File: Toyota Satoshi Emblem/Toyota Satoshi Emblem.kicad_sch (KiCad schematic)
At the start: 478 parts, among them J1 Conn_01x03_Male, J10 Ambient Harness, J11 Letter Terminal, J12 Letter Terminal, J13 Letter Terminal, J14 Letter Terminal, J15 Letter Terminal, J16 Letter Terminal, J17 Serial Terminal, J18 Power Port Terminal, J2 Conn_01x03_Male, J3 Conn_01x03_Male, J4 Conn_01x03_Male, J5 Conn_01x03_Male, J6 Conn_01x03_Male, J7 Conn_01x09_Male, J8 Conn_01x09_Female, J9 Serial Terminal, K1 FINDER-40.51, Q1 BC327, Q10 2N3904, Q11 IRLZ44N, Q12 IRLZ44N, Q13 IRLZ44N, Q14 IRLZ44N, Q15 IRLZ44N, Q16 IRLZ44N, Q17 IRLZ44N, Q18 IRLZ44N, Q19 IRLZ44N, Q2 BC337, Q20 IRLZ44N, Q21 2N3904, Q22 2N3904, Q23 2N3904, Q24 2N3904, Q25 2N3904, Q26 2N3904, Q27 IRLZ44N, Q28 IRLZ44N, Q29 IRLZ44N, Q3 IRF4905, Q30 IRLZ44N, Q31 IRLZ44N, Q32 IRLZ44N, Q33 IRLZ44N, Q34 IRLZ44N, Q35 IRLZ44N, Q36 IRLZ44N, Q37 IRLZ44N, Q38 IRLZ44N, Q4 IRLZ44N, Q5 IRLZ44N, Q6 IRLZ44N, Q7 IRLZ44N, Q8 IRLZ44N, Q9 IRLZ44N, U1 LM2596S-ADJ, U2 LM2596S-ADJ, U3 L7805, U4 LM2596S-ADJ, U5 LM2596S-ADJ

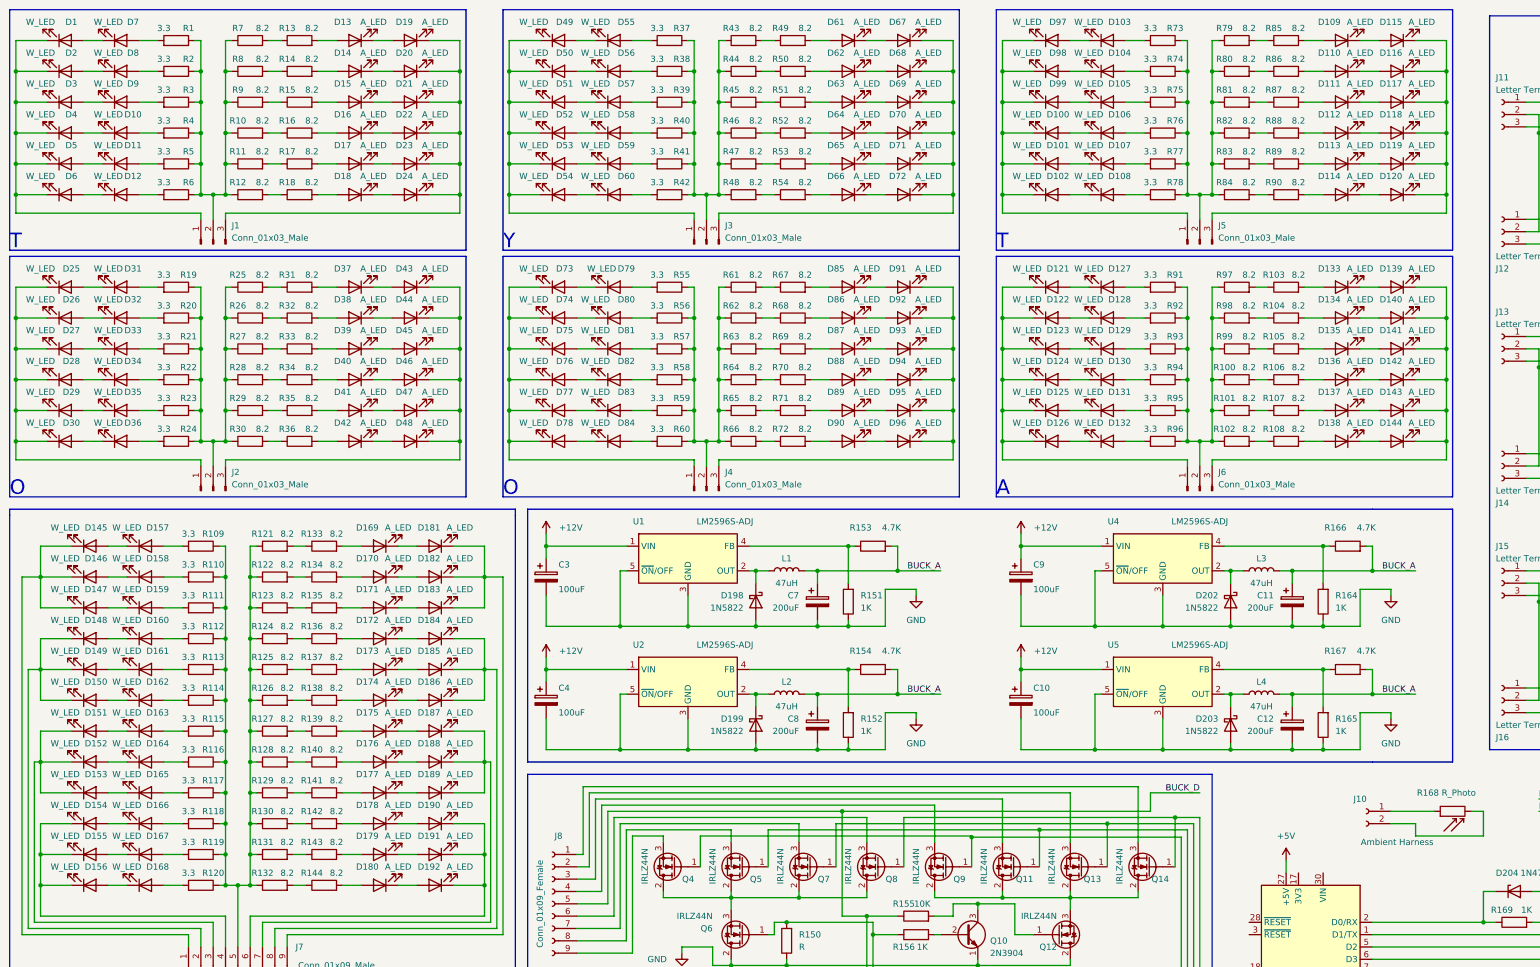
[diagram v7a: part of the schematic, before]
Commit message: v1.8
Letter T is now complete
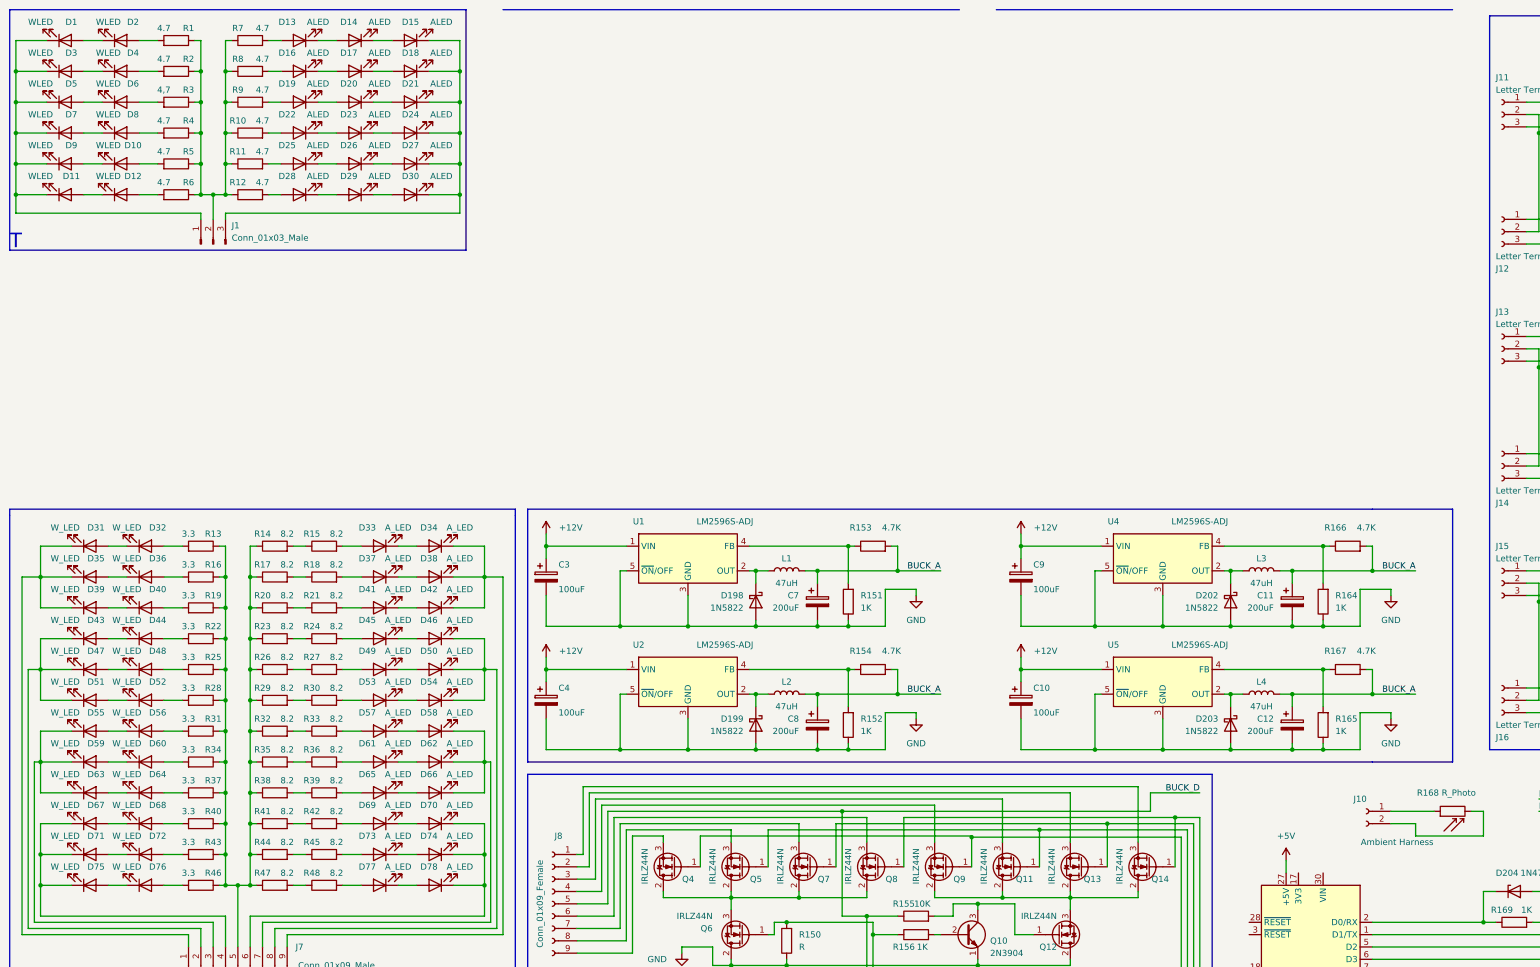
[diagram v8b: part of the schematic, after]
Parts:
- removed D100, D101, D102, D103, D104, D105, D106, D107, D108, D121, D122, D123, D124, D125, D126, D127, D128, D129, D130, D131, D132, D26, D27, D29, D30, D31, D32, D33, D34, D35, D36, D49, D50, D51, D52, D53, D54, D55, D56, D57, D58, D59, D60, D73, D74, D75, D76, D77, D78, D79, D80, D81, D82, D83, D84, D97, D98, D99: W_LED, afootprints:5730 LED W, symbol Device:LED
- removed D109, D110, D111, D112, D113, D114, D115, D116, D117, D118, D119, D120, D133, D134, D135, D136, D137, D138, D139, D140, D141, D142, D143, D144, D37, D38, D39, D40, D41, D42, D43, D44, D45, D46, D47, D48, D61, D62, D63, D64, D65, D66, D67, D68, D69, D70, D71, D72, D85, D86, D87, D88, D89, D90, D91, D92, D93, D94, D95, D96: A_LED, afootprints:5730 LED A, symbol Device:LED
- removed J2, J3, J4, J5, J6: Conn_01x03_Male, symbol Connector:Conn_01x03_Male
- removed R100, R101, R102, R103, R104, R105, R106, R107, R108, R13, R14, R15, R16, R17, R18, R25, R26, R27, R28, R29, R30, R31, R32, R33, R34, R35, R36, R43, R44, R45, R46, R47, R48, R49, R50, R51, R52, R53, R54, R61, R62, R63, R64, R65, R66, R67, R68, R69, R70, R71, R72, R79, R80, R81, R82, R83, R84, R85, R86, R87, R88, R89, R90, R97, R98, R99: 8.2, afootprints:1206 R, symbol Device:R
- removed R19, R20, R21, R22, R23, R24, R37, R38, R39, R40, R41, R42, R55, R56, R57, R58, R59, R60, R73, R74, R75, R76, R77, R78, R91, R92, R93, R94, R95, R96: 3.3, afootprints:1206 R, symbol Device:R
- added D13, D16, D19, D22: ALED, afootprints:5730 LED A, symbol Device:LED
- D1, D12: value W_LED -> WLED
- D10: renamed from D11; value W_LED -> WLED
- D11: renamed from D6; value W_LED -> WLED
- D14: renamed from D13; value A_LED -> ALED
- D15: renamed from D19; value A_LED -> ALED
- D17: renamed from D14; value A_LED -> ALED
- D18: renamed from D20; value A_LED -> ALED
- D2: renamed from D7; value W_LED -> WLED
- D20: renamed from D15; value A_LED -> ALED
- D21: value A_LED -> ALED
- D23: renamed from D16; value A_LED -> ALED
- D24: renamed from D22; value A_LED -> ALED
- D25, D28: value W_LED -> ALED; footprint afootprints:5730 LED W -> afootprints:5730 LED A
- D26: renamed from D17; value A_LED -> ALED
- D27: renamed from D23; value A_LED -> ALED
- D29: renamed from D18; value A_LED -> ALED
- D3: renamed from D2; value W_LED -> WLED
- D30: renamed from D24; value A_LED -> ALED
- D31: renamed from D145; footprint afootprints:5730 LED W -> (none)
- D32: renamed from D157; footprint afootprints:5730 LED W -> (none)
- D33: renamed from D169; footprint afootprints:5730 LED A -> (none)
- D34: renamed from D181; footprint afootprints:5730 LED A -> (none)
- D35: renamed from D146; footprint afootprints:5730 LED W -> (none)
- D36: renamed from D158; footprint afootprints:5730 LED W -> (none)
- D37: renamed from D170; footprint afootprints:5730 LED A -> (none)
- D38: renamed from D182; footprint afootprints:5730 LED A -> (none)
- D39: renamed from D147; footprint afootprints:5730 LED W -> (none)
- D4: renamed from D8; value W_LED -> WLED
- D40: renamed from D159; footprint afootprints:5730 LED W -> (none)
- D41: renamed from D171; footprint afootprints:5730 LED A -> (none)
- D42: renamed from D183; footprint afootprints:5730 LED A -> (none)
- D43: renamed from D148; footprint afootprints:5730 LED W -> (none)
- D44: renamed from D160; footprint afootprints:5730 LED W -> (none)
- D45: renamed from D172; footprint afootprints:5730 LED A -> (none)
- D46: renamed from D184; footprint afootprints:5730 LED A -> (none)
- D47: renamed from D149; footprint afootprints:5730 LED W -> (none)
- D48: renamed from D161; footprint afootprints:5730 LED W -> (none)
- D49: renamed from D173; footprint afootprints:5730 LED A -> (none)
- D5: renamed from D3; value W_LED -> WLED
- D50: renamed from D185; footprint afootprints:5730 LED A -> (none)
- D51: renamed from D150; footprint afootprints:5730 LED W -> (none)
- D52: renamed from D162; footprint afootprints:5730 LED W -> (none)
- D53: renamed from D174; footprint afootprints:5730 LED A -> (none)
- D54: renamed from D186; footprint afootprints:5730 LED A -> (none)
- D55: renamed from D151; footprint afootprints:5730 LED W -> (none)
- D56: renamed from D163; footprint afootprints:5730 LED W -> (none)
- D57: renamed from D175; footprint afootprints:5730 LED A -> (none)
- D58: renamed from D187; footprint afootprints:5730 LED A -> (none)
- D59: renamed from D152; footprint afootprints:5730 LED W -> (none)
- D6: renamed from D9; value W_LED -> WLED
- D60: renamed from D164; footprint afootprints:5730 LED W -> (none)
- D61: renamed from D176; footprint afootprints:5730 LED A -> (none)
- D62: renamed from D188; footprint afootprints:5730 LED A -> (none)
- D63: renamed from D153; footprint afootprints:5730 LED W -> (none)
- D64: renamed from D165; footprint afootprints:5730 LED W -> (none)
- D65: renamed from D177; footprint afootprints:5730 LED A -> (none)
- D66: renamed from D189; footprint afootprints:5730 LED A -> (none)
- D67: renamed from D154; footprint afootprints:5730 LED W -> (none)
- D68: renamed from D166; footprint afootprints:5730 LED W -> (none)
- D69: renamed from D178; footprint afootprints:5730 LED A -> (none)
- D7: renamed from D4; value W_LED -> WLED
- D70: renamed from D190; footprint afootprints:5730 LED A -> (none)
- D71: renamed from D155; footprint afootprints:5730 LED W -> (none)
- D72: renamed from D167; footprint afootprints:5730 LED W -> (none)
- D73: renamed from D179; footprint afootprints:5730 LED A -> (none)
- D74: renamed from D191; footprint afootprints:5730 LED A -> (none)
- D75: renamed from D156; footprint afootprints:5730 LED W -> (none)
- D76: renamed from D168; footprint afootprints:5730 LED W -> (none)
- D77: renamed from D180; footprint afootprints:5730 LED A -> (none)
- D78: renamed from D192; footprint afootprints:5730 LED A -> (none)
- D8: renamed from D10; value W_LED -> WLED
- D9: renamed from D5; value W_LED -> WLED
- R1, R2, R4, R5, R6: value 3.3 -> 4.7
- R10, R11, R12, R7, R8, R9: value 8.2 -> 4.7
- R13: renamed from R109; footprint afootprints:1206 R -> (none)
- R14: renamed from R121; footprint afootprints:1206 R -> (none)
- R15: renamed from R133; footprint afootprints:1206 R -> (none)
- R16: renamed from R110; footprint afootprints:1206 R -> (none)
- R17: renamed from R122; footprint afootprints:1206 R -> (none)
- R18: renamed from R134; footprint afootprints:1206 R -> (none)
- R19: renamed from R111; footprint afootprints:1206 R -> (none)
- R20: renamed from R123; footprint afootprints:1206 R -> (none)
- R21: renamed from R135; footprint afootprints:1206 R -> (none)
- R22: renamed from R112; footprint afootprints:1206 R -> (none)
- R23: renamed from R124; footprint afootprints:1206 R -> (none)
- R24: renamed from R136; footprint afootprints:1206 R -> (none)
- R25: renamed from R113; footprint afootprints:1206 R -> (none)
- R26: renamed from R125; footprint afootprints:1206 R -> (none)
- R27: renamed from R137; footprint afootprints:1206 R -> (none)
- R28: renamed from R114; footprint afootprints:1206 R -> (none)
- R29: renamed from R126; footprint afootprints:1206 R -> (none)
- R3: value 3.3 -> 4,7
- R30: renamed from R138; footprint afootprints:1206 R -> (none)
- R31: renamed from R115; footprint afootprints:1206 R -> (none)
- R32: renamed from R127; footprint afootprints:1206 R -> (none)
- R33: renamed from R139; footprint afootprints:1206 R -> (none)
- R34: renamed from R116; footprint afootprints:1206 R -> (none)
- R35: renamed from R128; footprint afootprints:1206 R -> (none)
- R36: renamed from R140; footprint afootprints:1206 R -> (none)
- R37: renamed from R117; footprint afootprints:1206 R -> (none)
- R38: renamed from R129; footprint afootprints:1206 R -> (none)
- R39: renamed from R141; footprint afootprints:1206 R -> (none)
- R40: renamed from R118; footprint afootprints:1206 R -> (none)
- R41: renamed from R130; footprint afootprints:1206 R -> (none)
- R42: renamed from R142; footprint afootprints:1206 R -> (none)
- R43: renamed from R119; footprint afootprints:1206 R -> (none)
- R44: renamed from R131; footprint afootprints:1206 R -> (none)
- R45: renamed from R143; footprint afootprints:1206 R -> (none)
- R46: renamed from R120; footprint afootprints:1206 R -> (none)
- R47: renamed from R132; footprint afootprints:1206 R -> (none)
- R48: renamed from R144; footprint afootprints:1206 R -> (none)
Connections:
- net at D20.2 (A): now also D19.1 (K)
- net at R9.2: now also D19.2 (A)
- net at D25.1 (K): now also D26.2 (A); no longer D28.1 (K)
- net at D23.2 (A): now also D22.1 (K)
- net at R7.2: now also D13.2 (A)
- net at D25.2 (A): now also R11.2
- net at D14.2 (A): now also D13.1 (K)
- net at R12.2: now also D28.2 (A)
- net at R10.2: now also D22.2 (A)
- net at D29.2 (A): now also D28.1 (K)
- net at R8.2: now also D16.2 (A)
- net at D17.2 (A): now also D16.1 (K)
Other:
- note removed: "A"
- note removed: "O"
- note removed: "Y"
